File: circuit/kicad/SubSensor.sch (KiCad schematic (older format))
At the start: 5 parts, among them J1 SH3, U1 S7136

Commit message: hoge
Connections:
- net +5V: now also J1.1 (Pin_1); no longer J1.3 (Pin_3)
- net GND: now also J1.3 (Pin_3); no longer J1.1 (Pin_1)
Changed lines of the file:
@@
 $Descr A4 11693 8268
 encoding utf-8
-Sheet 5 5
+Sheet 1 1
 Title ""
 Date ""
@@
 F 3 "~" H 3050 4450 50  0001 C CNN
 	1    3050 4450
-	-1   0    0    1
+	-1   0    0    -1
 $EndComp
 Wire Wire Line

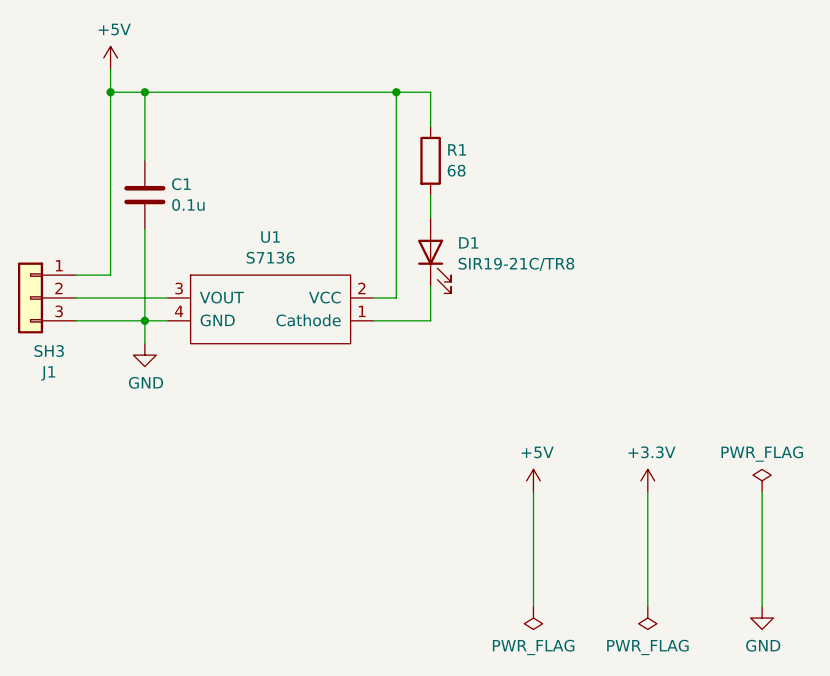
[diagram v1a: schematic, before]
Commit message: あとはシルクを見やすい位置にもっていくだけ。
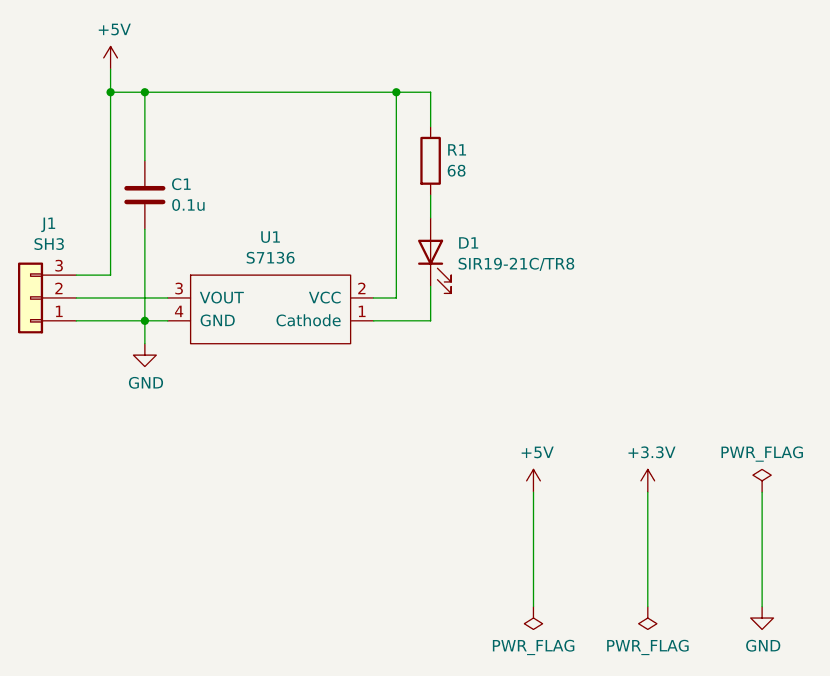
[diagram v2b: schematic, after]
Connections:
- net +5V: now also J1.3 (Pin_3); no longer J1.1 (Pin_1)
- net GND: now also J1.1 (Pin_1); no longer J1.3 (Pin_3)
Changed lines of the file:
@@
 F 3 "~" H 3050 4450 50  0001 C CNN
 	1    3050 4450
-	-1   0    0    -1
+	-1   0    0    1
 $EndComp
 Wire Wire Line
